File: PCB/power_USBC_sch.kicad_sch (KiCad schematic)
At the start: 17 parts, among them J1 USB4105, U3 LTC3405

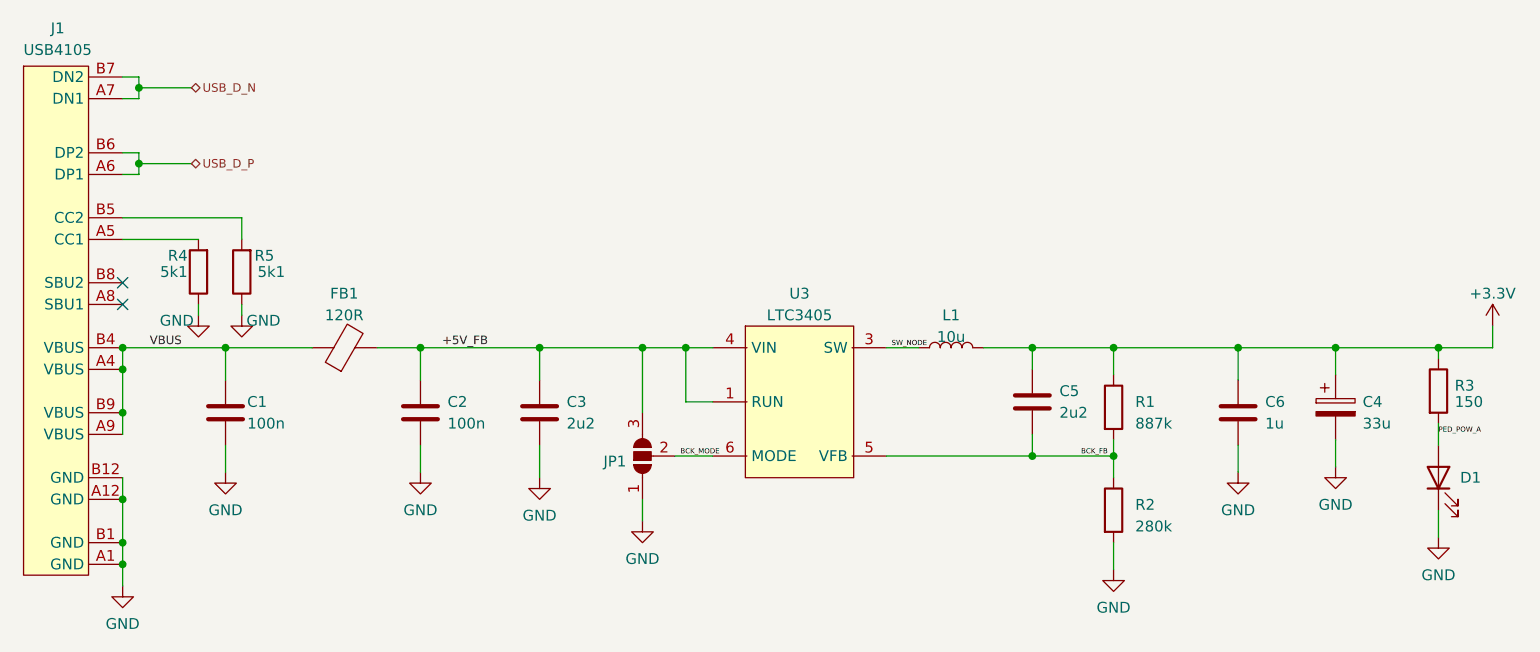
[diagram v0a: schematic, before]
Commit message: Layout complted, gerber files generated
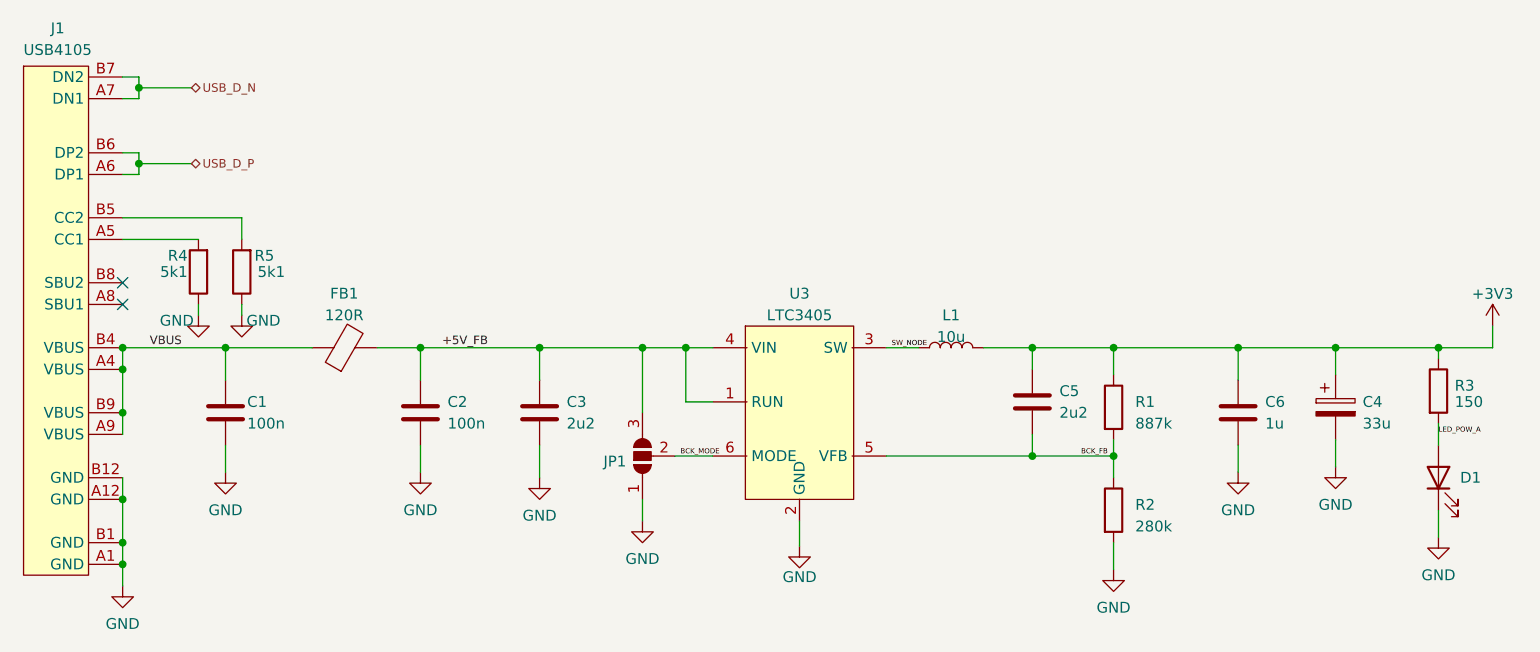
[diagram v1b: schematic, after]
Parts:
- C1, C2, C3, C5, C6: footprint (none) -> Capacitor_SMD:C_0603_1608Metric
- C4: footprint (none) -> Capacitor_SMD:C_1210_3225Metric
- D1: footprint (none) -> LED_SMD:LED_0805_2012Metric
- FB1, R1, R2, R3, R4, R5: footprint (none) -> Resistor_SMD:R_0603_1608Metric
- J1: footprint (none) -> User_Footprint:USBC_4105
- JP1: footprint (none) -> Jumper:SolderJumper-3_P1.3mm_Open_Pad1.0x1.5mm
- L1: footprint (none) -> Inductor_SMD:L_0805_2012Metric
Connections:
- net GND: now also U3.2 (GND)
- net +3.3V renamed +3V3
- net PED_POW_A renamed LED_POW_A
